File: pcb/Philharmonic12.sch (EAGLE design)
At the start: 45 parts, among them IC1 MC6821, IC2 AY-3-8910-RP, IC3 AY-3-8910-RP, IC4 AY-3-8910-RP, IC5 AY-3-8910-RP, IC6 74LS138N, IC7 74ALS30N, IC8 LM386N-1, IC9 LM386N-1, X1 EXPANSION_PORT_COCO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

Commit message: Can't get .895MHz oscillators, so modified to use 3.59MHz and /4 divider.
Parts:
- added C18: (no value), rcl:C-US025-025X050
- added IC10: 74LS74N, 74xx-us-jlb:74LS74N
- QG1: value .895MHz -> 3.579545MHz
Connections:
- new net N$1: IC10A.!Q, IC10A.D
- new net N$10: IC10A.Q, IC10B.CLK
- new net N$15: IC10B.!Q, IC10B.D
- new net N$17: CLK_SEL.1, IC10B.Q
- net GND: now also C18.2
- net N$4: now also IC10A.CLK; no longer CLK_SEL.1
- net VCC: now also C18.1, IC10A.CLR, IC10A.PRE, IC10B.CLR, IC10B.PRE
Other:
- moved on the sheet: CLK_SEL, QG1

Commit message: Added parts values
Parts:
- C1, C2, C3, C4, C7: value (none) -> 4m7
- C10, C11, C12, C13, C14, C15, C16, C17, C18, C8, C9: value (none) -> .1u
- C5, C6: value (none) -> 220p
- R1, R2, R3, R4: value (none) -> 470
- R10, R11, R12, R9: value (none) -> 10K
- R5, R6: value (none) -> 4K7
- R7, R8: value (none) -> 1K
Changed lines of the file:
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@@
 <part name="IC8" library="linear" deviceset="LM386?-*" device="N" technology="1"/>
 <part name="IC9" library="linear" deviceset="LM386?-*" device="N" technology="1"/>
-<part name="C1" library="rcl" deviceset="CPOL-US" device="E2.5-6"/>
-<part name="C2" library="rcl" deviceset="CPOL-US" device="E2.5-6"/>
+<part name="C1" library="rcl" deviceset="CPOL-US" device="E2.5-6" value="4m7"/>
+<part name="C2" library="rcl" deviceset="CPOL-US" device="E2.5-6" value="4m7"/>
 <part name="SUPPLY6" library="supply2" deviceset="GND" device=""/>
 <part name="SUPPLY7" library="supply2" deviceset="GND" device=""/>
@@
 <part name="SUPPLY10" library="supply2" deviceset="VCC" device=""/>
 <part name="SUPPLY11" library="supply2" deviceset="VCC" device=""/>
-<part name="R1" library="rcl" deviceset="R-US_" device="0204/7"/>
-<part name="R2" library="rcl" deviceset="R-US_" device="0204/7"/>
-<part name="R3" library="rcl" deviceset="R-US_" device="0204/7"/>
-<part name="R4" library="rcl" deviceset="R-US_" device="0204/7"/>
-<part name="R5" library="rcl" deviceset="R-US_" device="0204/7"/>
-<part name="R6" library="rcl" deviceset="R-US_" device="0204/7"/>
-<part name="R7" library="rcl" deviceset="R-US_" device="0204/7"/>
-<part name="R8" library="rcl" deviceset="R-US_" device="0204/7"/>
-<part name="R9" library="rcl" deviceset="R-US_" device="0204/7"/>
-<part name="R10" library="rcl" deviceset="R-US_" device="0204/7"/>
-<part name="R11" library="rcl" deviceset="R-US_" device="0204/7"/>
-<part name="R12" library="rcl" deviceset="R-US_" device="0204/7"/>
-<part name="C3" library="rcl" deviceset="CPOL-US" device="E2.5-6"/>
-<part name="C4" library="rcl" deviceset="CPOL-US" device="E2.5-6"/>
-<part name="C5" library="rcl" deviceset="C-US" device="025-025X050"/>
-<part name="C6" library="rcl" deviceset="C-US" device="025-025X050"/>
+<part name="R1" library="rcl" deviceset="R-US_" device="0204/7" value="470"/>
+<part name="R2" library="rcl" deviceset="R-US_" device="0204/7" value="470"/>
+<part name="R3" library="rcl" deviceset="R-US_" device="0204/7" value="470"/>
+<part name="R4" library="rcl" deviceset="R-US_" device="0204/7" value="470"/>
+<part name="R5" library="rcl" deviceset="R-US_" device="0204/7" value="4K7"/>
+<part name="R6" library="rcl" deviceset="R-US_" device="0204/7" value="4K7"/>
+<part name="R7" library="rcl" deviceset="R-US_" device="0204/7" value="1K"/>
+<part name="R8" library="rcl" deviceset="R-US_" device="0204/7" value="1K"/>
+<part name="R9" library="rcl" deviceset="R-US_" device="0204/7" value="10K"/>
+<part name="R10" library="rcl" deviceset="R-US_" device="0204/7" value="10K"/>
+<part name="R11" library="rcl" deviceset="R-US_" device="0204/7" value="10K"/>
+<part name="R12" library="rcl" deviceset="R-US_" device="0204/7" value="10K"/>
+<part name="C3" library="rcl" deviceset="CPOL-US" device="E2.5-6" value="4m7"/>
+<part name="C4" library="rcl" deviceset="CPOL-US" device="E2.5-6" value="4m7"/>
+<part name="C5" library="rcl" deviceset="C-US" device="025-025X050" value="220p"/>
+<part name="C6" library="rcl" deviceset="C-US" device="025-025X050" value="220p"/>
 <part name="SUPPLY12" library="supply2" deviceset="GND" device=""/>
 <part name="SUPPLY13" library="supply2" deviceset="GND" device=""/>
@@
 <part name="SUPPLY16" library="supply2" deviceset="GND" device=""/>
 <part name="SUPPLY17" library="supply2" deviceset="GND" device=""/>
-<part name="C7" library="rcl" deviceset="CPOL-US" device="E2.5-6"/>
+<part name="C7" library="rcl" deviceset="CPOL-US" device="E2.5-6" value="4m7"/>
 <part name="SUPPLY18" library="supply2" deviceset="VCC" device=""/>
 <part name="SUPPLY19" library="supply2" deviceset="GND" device=""/>
@@
 <part name="SUPPLY22" library="supply2" deviceset="GND" device=""/>
 <part name="MONO" library="jumper-jlb" deviceset="JP1Q" device=""/>
-<part name="C8" library="rcl" deviceset="C-US" device="025-025X050"/>
-<part name="C9" library="rcl" deviceset="C-US" device="025-025X050"/>
-<part name="C10" library="rcl" deviceset="C-US" device="025-025X050"/>
-<part name="C11" library="rcl" deviceset="C-US" device="025-025X050"/>
-<part name="C12" library="rcl" deviceset="C-US" device="025-025X050"/>
-<part name="C13" library="rcl" deviceset="C-US" device="025-025X050"/>
-<part name="C14" library="rcl" deviceset="C-US" device="025-025X050"/>
-<part name="C15" library="rcl" deviceset="C-US" device="025-025X050"/>
-<part name="C16" library="rcl" deviceset="C-US" device="025-025X050"/>
+<part name="C8" library="rcl" deviceset="C-US" device="025-025X050" value=".1u"/>
+<part name="C9" library="rcl" deviceset="C-US" device="025-025X050" value=".1u"/>
+<part name="C10" library="rcl" deviceset="C-US" device="025-025X050" value=".1u"/>
+<part name="C11" library="rcl" deviceset="C-US" device="025-025X050" value=".1u"/>
+<part name="C12" library="rcl" deviceset="C-US" device="025-025X050" value=".1u"/>
+<part name="C13" library="rcl" deviceset="C-US" device="025-025X050" value=".1u"/>
+<part name="C14" library="rcl" deviceset="C-US" device="025-025X050" value=".1u"/>
+<part name="C15" library="rcl" deviceset="C-US" device="025-025X050" value=".1u"/>
+<part name="C16" library="rcl" deviceset="C-US" device="025-025X050" value=".1u"/>
 <part name="SUPPLY23" library="supply2" deviceset="VCC" device=""/>
 <part name="SUPPLY24" library="supply2" deviceset="VCC" device=""/>
@@
 <part name="SUPPLY58" library="supply2" deviceset="GND" device=""/>
 <part name="SUPPLY59" library="supply2" deviceset="GND" device=""/>
-<part name="C17" library="rcl" deviceset="C-US" device="025-025X050"/>
+<part name="C17" library="rcl" deviceset="C-US" device="025-025X050" value=".1u"/>
 <part name="SUPPLY60" library="supply2" deviceset="VCC" device=""/>
 <part name="SUPPLY61" library="supply2" deviceset="GND" device=""/>
@@
 <part name="SUPPLY64" library="supply2" deviceset="VCC" device=""/>
 <part name="SUPPLY65" library="supply2" deviceset="VCC" device=""/>
-<part name="C18" library="rcl" deviceset="C-US" device="025-025X050"/>
+<part name="C18" library="rcl" deviceset="C-US" device="025-025X050" value=".1u"/>
 <part name="SUPPLY66" library="supply2" deviceset="VCC" device=""/>
 <part name="SUPPLY67" library="supply2" deviceset="GND" device=""/>
@@
 </sheet>
 </sheets>
+<errors>
+</errors>
 </schematic>
 </drawing>

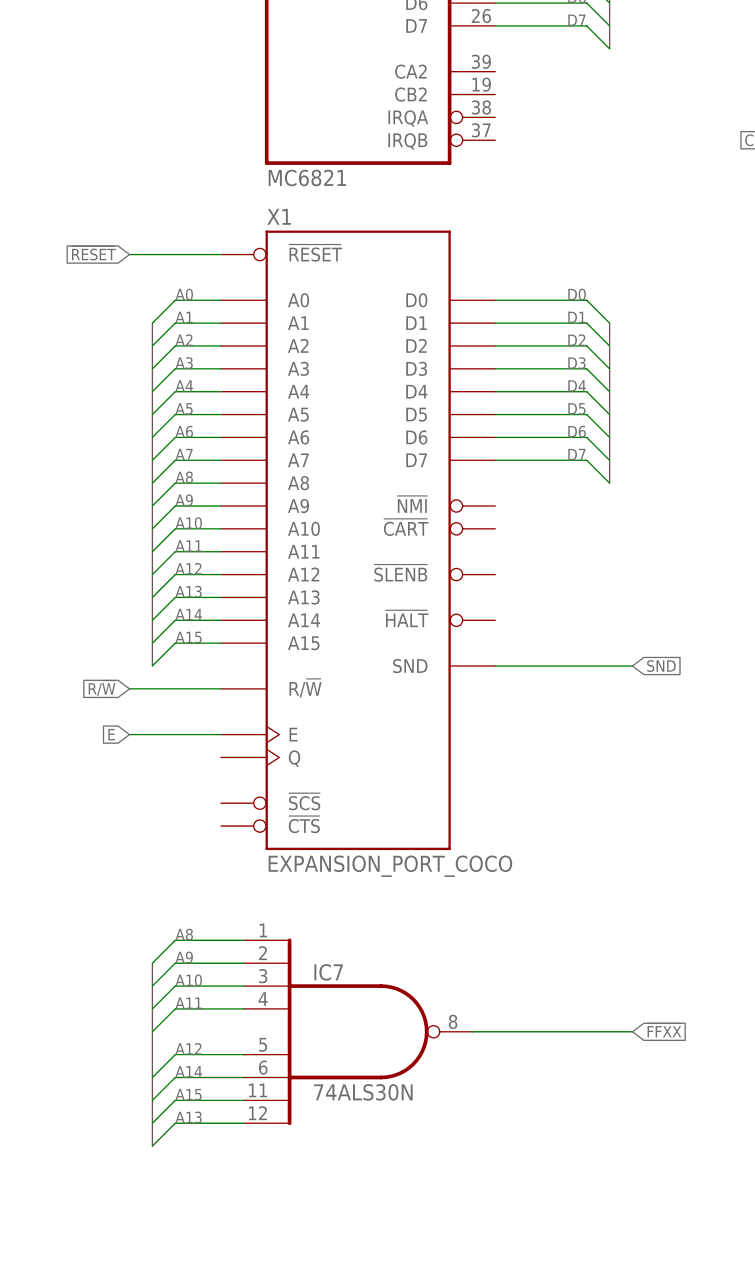
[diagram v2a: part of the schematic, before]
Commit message: Minor silkscreen updates
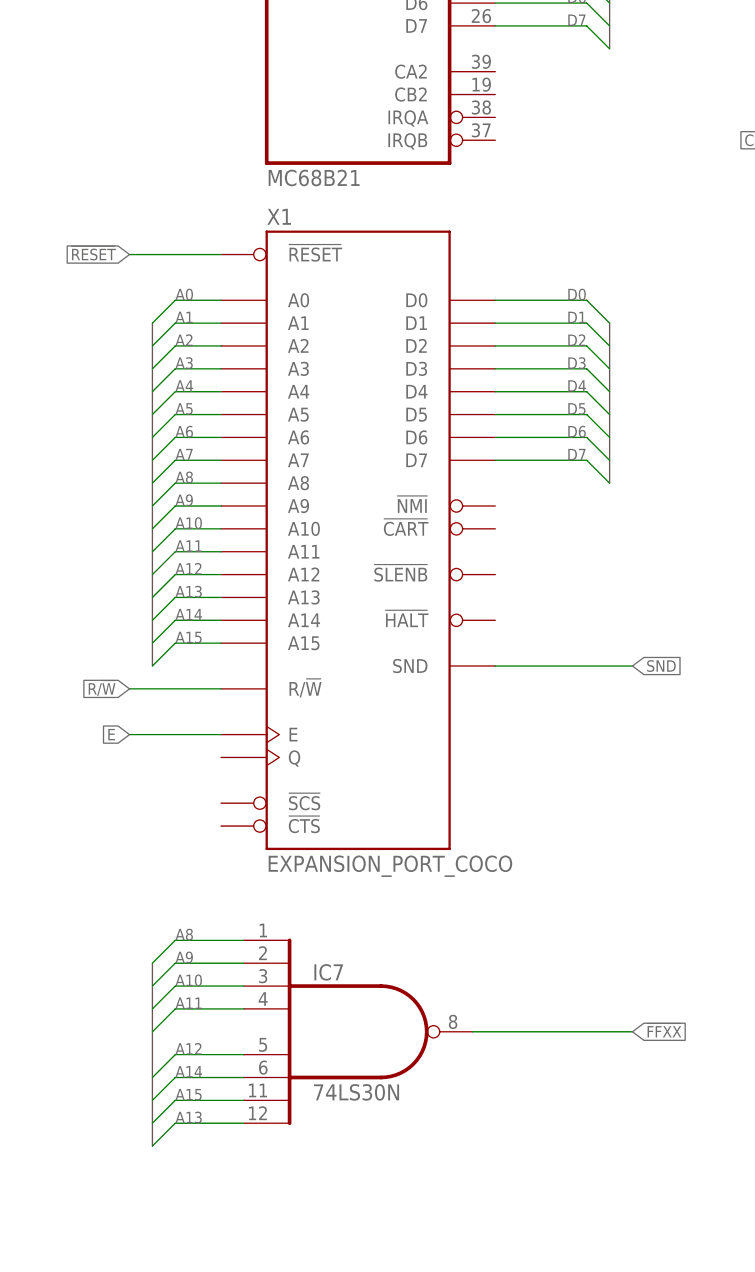
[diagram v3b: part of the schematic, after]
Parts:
- IC1: value MC6821 -> MC68B21
- IC7: value 74ALS30N -> 74LS30N
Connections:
- net N$10 renamed CLK/2
- net N$17 renamed CLK/4
- net N$4 renamed CLK
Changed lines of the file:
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@@
 </classes>
 <parts>
-<part name="IC1" library="micro-motorola" deviceset="6821" device="R" value="MC6821"/>
+<part name="IC1" library="micro-motorola" deviceset="6821" device="R" value="MC68B21"/>
 <part name="IC2" library="general-instrument" deviceset="AY-3-8910" device="-RP"/>
 <part name="IC3" library="general-instrument" deviceset="AY-3-8910" device="-RP"/>
@@
 <part name="SUPPLY3" library="supply2" deviceset="VCC" device=""/>
 <part name="SUPPLY4" library="supply2" deviceset="VCC" device=""/>
-<part name="IC7" library="74xx-us-jlb" deviceset="74*30" device="N" technology="ALS"/>
+<part name="IC7" library="74xx-us-jlb" deviceset="74*30" device="N" technology="ALS" value="74LS30N"/>
 <part name="SUPPLY5" library="supply2" deviceset="VCC" device=""/>
 <part name="FRAME2" library="frames" deviceset="FRAME_B_L" device=""/>
@@
 </segment>
 </net>
-<net name="N$4" class="0">
+<net name="CLK" class="0">
 <segment>
 <pinref part="QG1" gate="1" pin="OUT"/>
@@
 </segment>
 </net>
-<net name="N$10" class="0">
+<net name="CLK/2" class="0">
 <segment>
 <pinref part="IC10" gate="A" pin="Q"/>
@@
 </segment>
 </net>
-<net name="N$17" class="0">
+<net name="CLK/4" class="0">
 <segment>
 <pinref part="IC10" gate="B" pin="Q"/>
